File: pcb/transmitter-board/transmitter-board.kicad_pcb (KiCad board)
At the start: 2 copper layers, 0 parts

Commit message: Add transmitter-board schematics
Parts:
- added BT1: Battery, Battery:BatteryHolder_Keystone_1042_1x18650, F.Cu at (60.6, 42.8)
- added C1: 1n, Capacitor_SMD:C_0805_2012Metric_Pad1.18x1.45mm_HandSolder, F.Cu at (45.8, 60.7)
- added C2: 10n, Capacitor_SMD:C_0805_2012Metric_Pad1.18x1.45mm_HandSolder, F.Cu at (45.8, 63.7)
- added C4: 0.1u, Capacitor_SMD:C_0805_2012Metric_Pad1.18x1.45mm_HandSolder, F.Cu at (45.8, 66.7)
- added C6: 0.1u, Capacitor_SMD:C_0805_2012Metric_Pad1.18x1.45mm_HandSolder, F.Cu at (45.8, 69.7)
- added C7: 10u, Capacitor_SMD:C_0805_2012Metric_Pad1.18x1.45mm_HandSolder, F.Cu at (45.8, 72.7)
- added D1: R LED, LED_SMD:LED_0805_2012Metric_Pad1.15x1.40mm_HandSolder, F.Cu at (45.8, 75.8)
- added D2: B LED, LED_SMD:LED_0805_2012Metric_Pad1.15x1.40mm_HandSolder, F.Cu at (45.8, 78.8)
- added D5: IR LED, LED_THT:LED_D1.8mm_W1.8mm_H2.4mm_Horizontal_O3.81mm_Z8.2mm, F.Cu at (25.4, 66.0)
- added J1: USB_C_Receptacle_PowerOnly_6P, Connector_USB:USB_C_Receptacle_GCT_USB4125-xx-x-0190_6P_TopMnt_Horizontal, F.Cu at (54.1, 77.9)
- added Q1: BC817, Package_TO_SOT_SMD:SOT-23, F.Cu at (50.7, 61.6)
- added Q3: AO3400A, Package_TO_SOT_SMD:SOT-23, F.Cu at (50.7, 66.2)
- added Q4: AO3400A, Package_TO_SOT_SMD:SOT-23, F.Cu at (50.7, 70.8)
- added R1: 1k, Resistor_SMD:R_0805_2012Metric_Pad1.20x1.40mm_HandSolder, F.Cu at (36.3, 60.7)
- added R10: 100R, Resistor_SMD:R_0805_2012Metric_Pad1.20x1.40mm_HandSolder, F.Cu at (41.0, 66.6)
- added R11: 18, Resistor_SMD:R_0805_2012Metric_Pad1.20x1.40mm_HandSolder, F.Cu at (41.0, 69.5)
- added R12: 180, Resistor_SMD:R_0805_2012Metric_Pad1.20x1.40mm_HandSolder, F.Cu at (41.0, 72.5)
- added R2: 18.4k, Resistor_SMD:R_0805_2012Metric_Pad1.20x1.40mm_HandSolder, F.Cu at (36.3, 63.6)
- added R3: 5.1k, Resistor_SMD:R_0805_2012Metric_Pad1.20x1.40mm_HandSolder, F.Cu at (36.3, 66.6)
- added R4: 1k, Resistor_SMD:R_0805_2012Metric_Pad1.20x1.40mm_HandSolder, F.Cu at (36.3, 69.5)
- added R5: 1.2k, Resistor_SMD:R_0805_2012Metric_Pad1.20x1.40mm_HandSolder, F.Cu at (36.3, 72.5)
- added R6: 5.1k, Resistor_SMD:R_0805_2012Metric_Pad1.20x1.40mm_HandSolder, F.Cu at (36.3, 75.4)
- added R7: 1k, Resistor_SMD:R_0805_2012Metric_Pad1.20x1.40mm_HandSolder, F.Cu at (41.0, 60.7)
- added R9: 1k, Resistor_SMD:R_0805_2012Metric_Pad1.20x1.40mm_HandSolder, F.Cu at (41.0, 63.6)
- added U1: NE555D, Package_SO:SOIC-8_3.9x4.9mm_P1.27mm, F.Cu at (57.3, 62.5)
- added U3: TP4056-42-ESOP8, Package_SO:SOIC-8-1EP_3.9x4.9mm_P1.27mm_EP2.41x3.3mm_ThermalVias, F.Cu at (57.3, 69.1)
- added U4: DW01A, Package_TO_SOT_SMD:SOT-23-6, F.Cu at (36.5, 79.3)

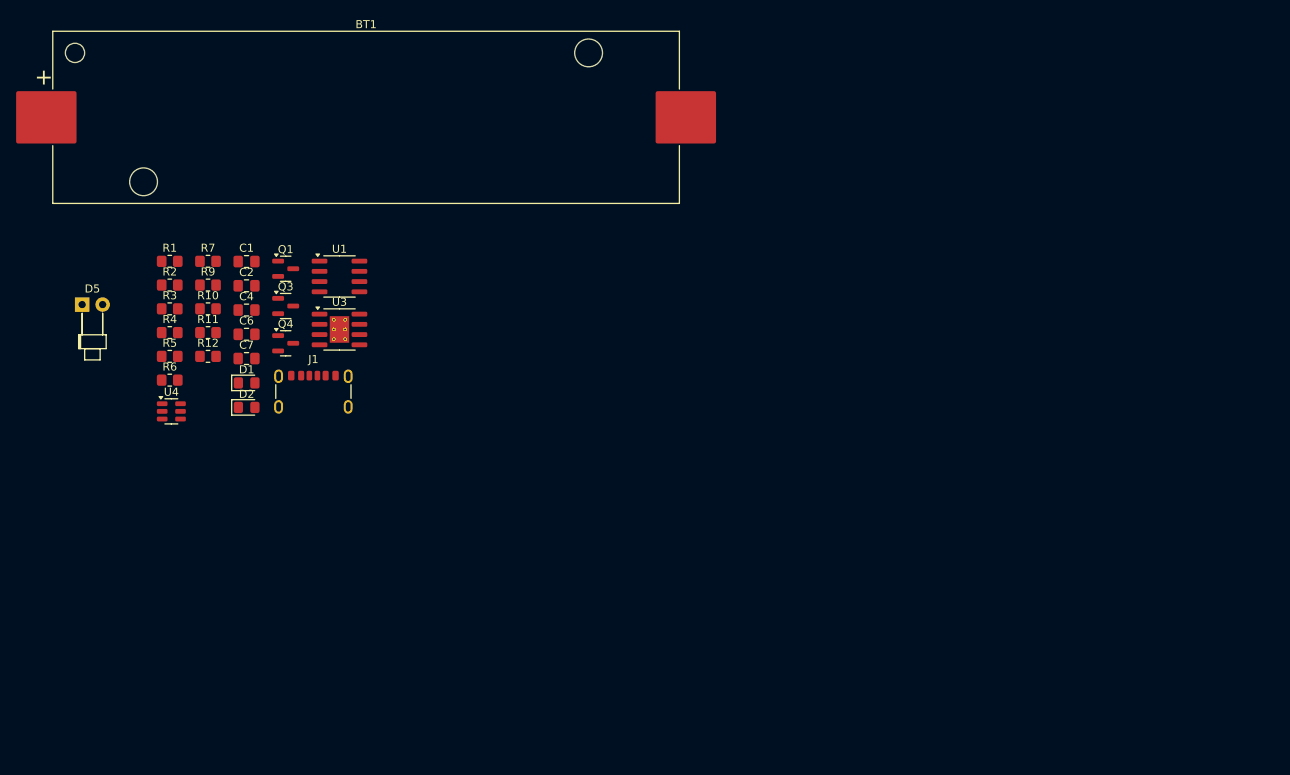
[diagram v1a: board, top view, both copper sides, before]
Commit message: Add transmitter-board pcb
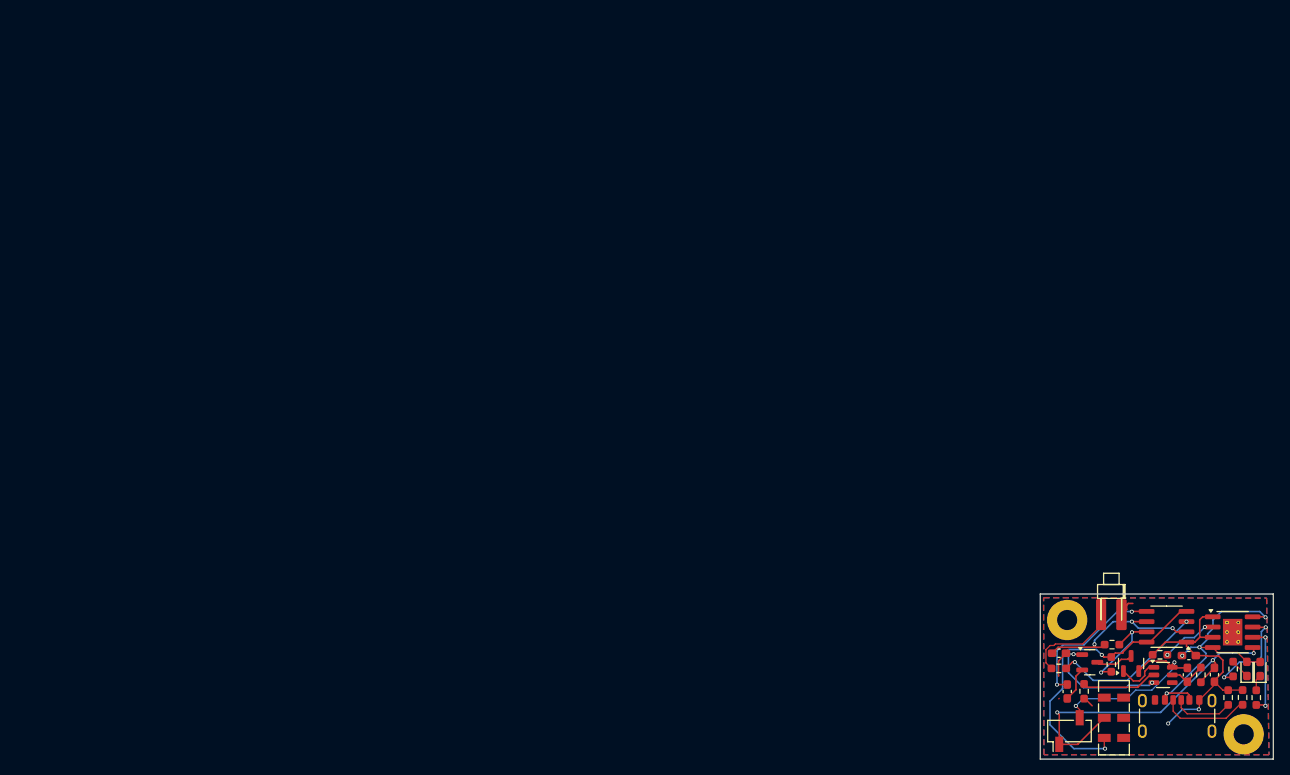
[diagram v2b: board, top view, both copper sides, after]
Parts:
- removed D5: IR LED, LED_THT:LED_D1.8mm_W1.8mm_H2.4mm_Horizontal_O3.81mm_Z8.2mm
- removed Q1: BC817, Package_TO_SOT_SMD:SOT-23
- removed R11: 18, Resistor_SMD:R_0805_2012Metric_Pad1.20x1.40mm_HandSolder
- removed R12: 180, Resistor_SMD:R_0805_2012Metric_Pad1.20x1.40mm_HandSolder
- added D3: IR LED, LED_THT:LED_THT_Horizontal_SMD_mounted, F.Cu at (154.4, 106.3)
- added R8: 150, Resistor_SMD:R_0603_1608Metric_Pad0.98x0.95mm_HandSolder, F.Cu at (146.6, 111.2)
- added REF**: MountingHole_2.5mm_Pad, MountingHole:MountingHole_2.5mm_Pad, F.Cu at (147.7, 105.2)
- added REF**: MountingHole_2.5mm_Pad, MountingHole:MountingHole_2.5mm_Pad, F.Cu at (169.6, 119.4)
- added SW1: SW_DPDT_x2, Button_Switch_SMD:SW_DPDT_CK_JS202011JCQN, F.Cu at (153.5, 117.3)
- BT1: footprint Battery:BatteryHolder_Keystone_1042_1x18650 -> Connector_PinSocket_2.54mm:PinSocket_1x02_P2.54mm_Vertical_SMD_Pin1Left
- C1, C2, C4, C6, C7: footprint Capacitor_SMD:C_0805_2012Metric_Pad1.18x1.45mm_HandSolder -> Capacitor_SMD:C_0603_1608Metric_Pad1.08x0.95mm_HandSolder
- D1, D2: footprint LED_SMD:LED_0805_2012Metric_Pad1.15x1.40mm_HandSolder -> LED_SMD:LED_0603_1608Metric_Pad1.05x0.95mm_HandSolder
- R1, R10, R2, R3, R4, R5, R6, R7, R9: footprint Resistor_SMD:R_0805_2012Metric_Pad1.20x1.40mm_HandSolder -> Resistor_SMD:R_0603_1608Metric_Pad0.98x0.95mm_HandSolder
- moved R4 142.3 mm to (171.1, 114.8), turned to 90 degrees
- moved R3 140.0 mm to (167.6, 114.8), turned to 90 degrees
- moved R6 138.9 mm to (169.4, 114.8), turned to 90 degrees
- moved R7 136.9 mm to (168.3, 111.3), turned to 90 degrees
- moved R10 131.3 mm to (164.3, 112.0), turned to 90 degrees
- moved D2 129.9 mm to (171.6, 111.3), turned to 90 degrees
- moved D1 129.1 mm to (170.0, 111.3), turned to 90 degrees
- moved R5 128.4 mm to (159.2, 109.5), turned to 180 degrees
- moved U4 127.4 mm to (159.6, 112.0)
- moved R1 127.1 mm to (153.1, 110.7), turned to -90 degrees
- moved C7 126.4 mm to (165.9, 112.0), turned to -90 degrees
- moved R2 125.2 mm to (153.2, 108.3), turned to 180 degrees
- moved C4 124.6 mm to (162.8, 109.6)
- moved C6 124.2 mm to (162.6, 112.0), turned to 90 degrees
- moved R9 119.9 mm to (149.8, 114.0), turned to -90 degrees
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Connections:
- BT1 pad 2: GND -> /B-
- C6 pad 2: GND -> /B-
- J1 pad S1: unconnected-(J1-SHIELD-PadS1) -> GND
- Q4 pad 2: GND -> /B-
- R1 pad 1: +3V8 -> Net-(SW1A-A)
- U1 pad 4: +3V8 -> Net-(SW1A-A)
- U1 pad 8: +3V8 -> Net-(SW1A-A)
- U4 pad 6: GND -> /B-
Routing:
- net GND: track 0.00 -> 45.2 mm, vias 0 -> 2
- net +3V8: track 0.00 -> 42.8 mm, vias 0 -> 3
- net Net-(SW1A-A): track 0.00 -> 37.2 mm, vias 0 -> 2
- net /IN+: track 0.00 -> 36.6 mm, vias 0 -> 4
- net /B-: track 0.00 -> 24.2 mm, vias 0 -> 2
- net Net-(U1-THR): track 0.00 -> 23.0 mm, vias 0 -> 3
- net /555OUT: track 0.00 -> 19.2 mm, vias 0 -> 2
- net Net-(U1-CV): track 0.00 -> 18.7 mm, vias 0 -> 2
- net Net-(Q3-G): track 0.00 -> 15.5 mm, vias 0 -> 2
- net Net-(U3-~{CHRG}): track 0.00 -> 12.4 mm, vias 0 -> 2
- net Net-(D3-A): track 0.00 -> 12.1 mm
- net Net-(U1-DIS): track 0.00 -> 11.9 mm, vias 0 -> 2
- net Net-(U3-~{STDBY}): track 0.00 -> 11.3 mm, vias 0 -> 2
- net Net-(J1-CC1): track 0.00 -> 11.1 mm
- net Net-(U4-CS): track 0.00 -> 9.47 mm
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- added copper zone on B.Cu, net GND
- added copper zone on F.Cu, net GND
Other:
- board outline added: 28.9 x 20.5 mm

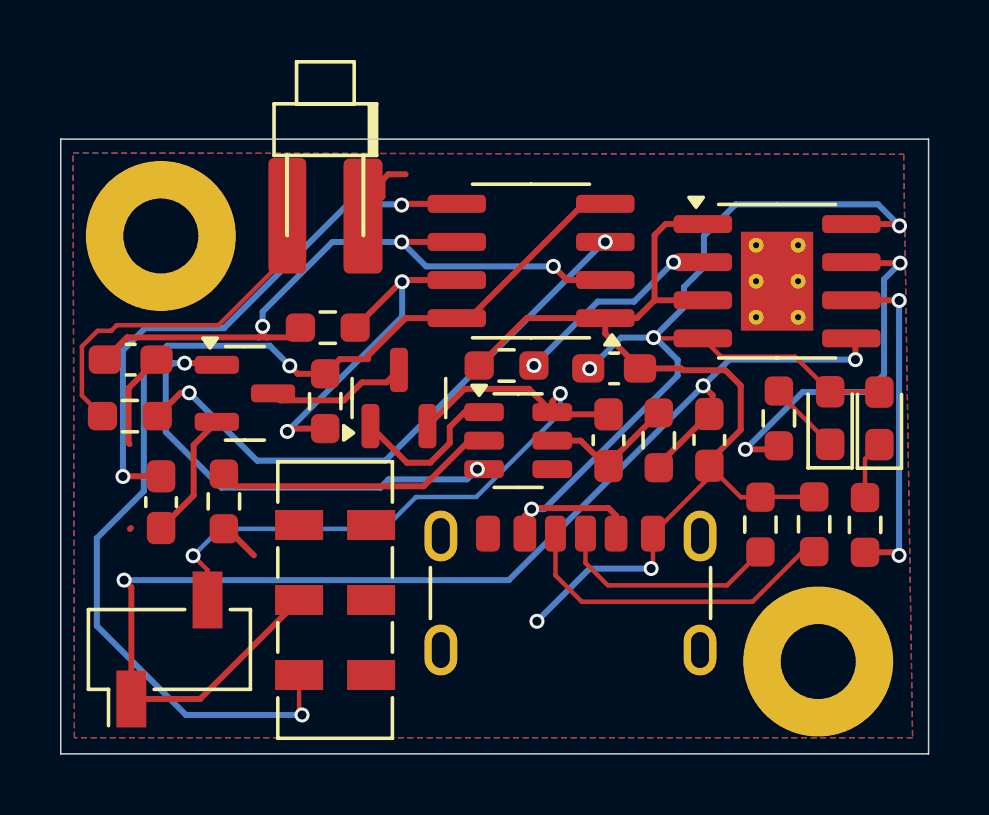
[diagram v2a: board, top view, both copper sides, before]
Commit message: Change hole size under TP4056 and change battery connector to THT.
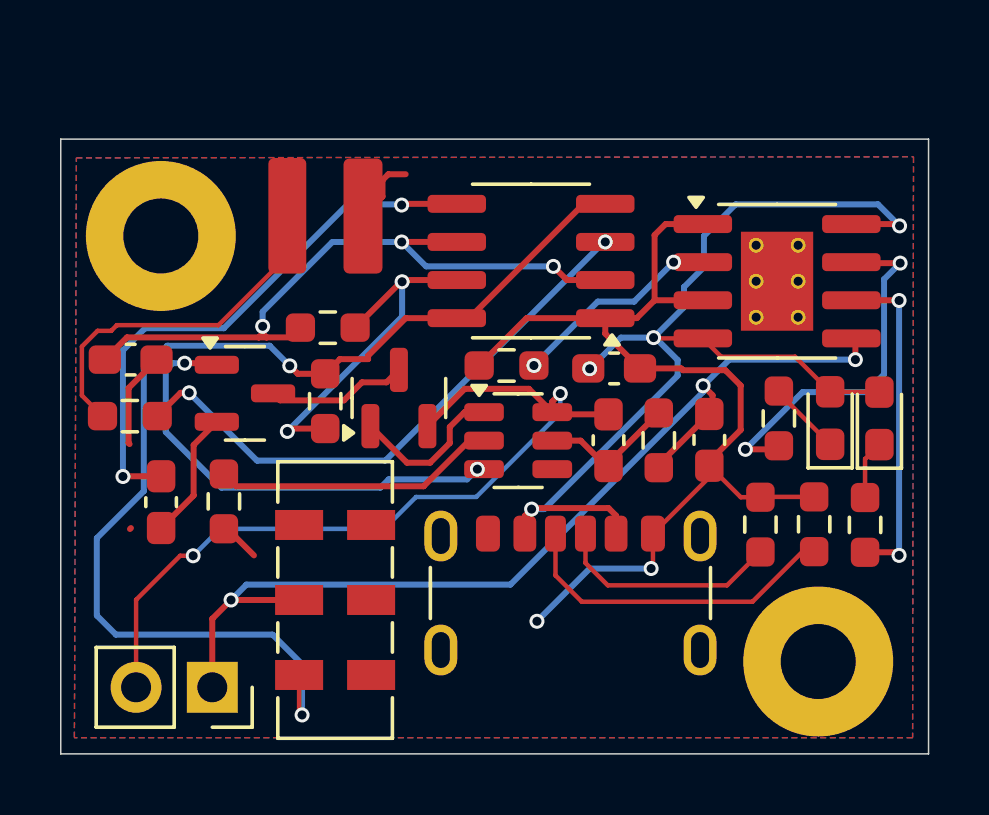
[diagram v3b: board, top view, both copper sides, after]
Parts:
- BT1: footprint Connector_PinSocket_2.54mm:PinSocket_1x02_P2.54mm_Vertical_SMD_Pin1Left -> Connector_PinSocket_2.54mm:PinSocket_1x02_P2.54mm_Vertical
- moved BT1 1.91 mm to (149.4, 120.2), turned to -90 degrees
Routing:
- net +3V8: track 42.8 -> 34.1 mm
- net /B-: track 24.2 -> 27.9 mm
- net Net-(SW1A-A): track 37.2 -> 38.0 mm

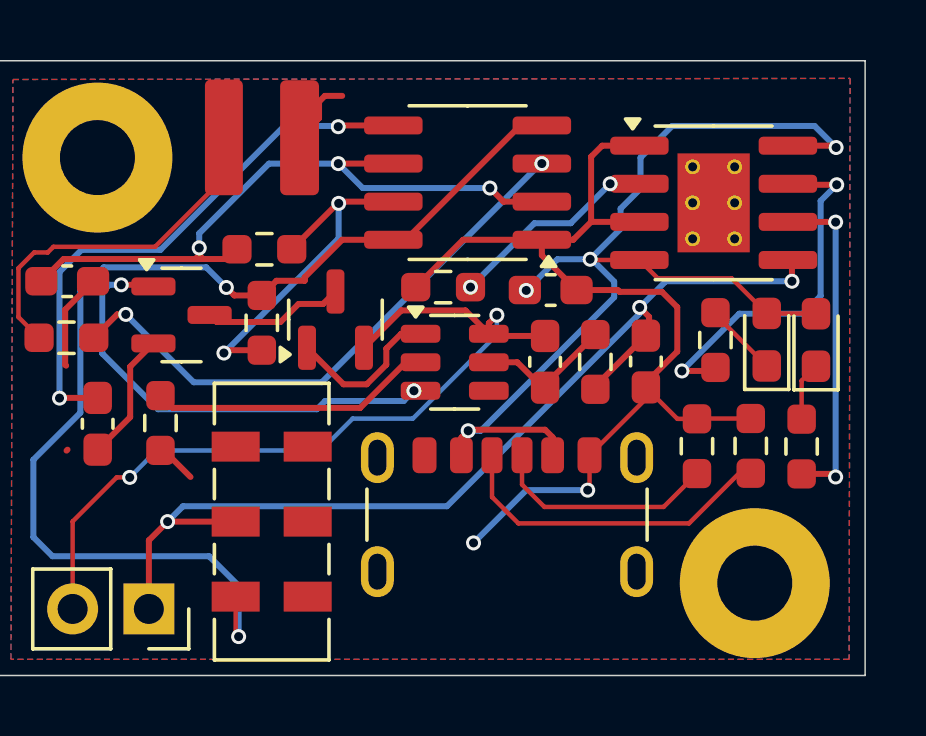
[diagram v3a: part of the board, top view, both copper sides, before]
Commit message: Change USB and battery connector
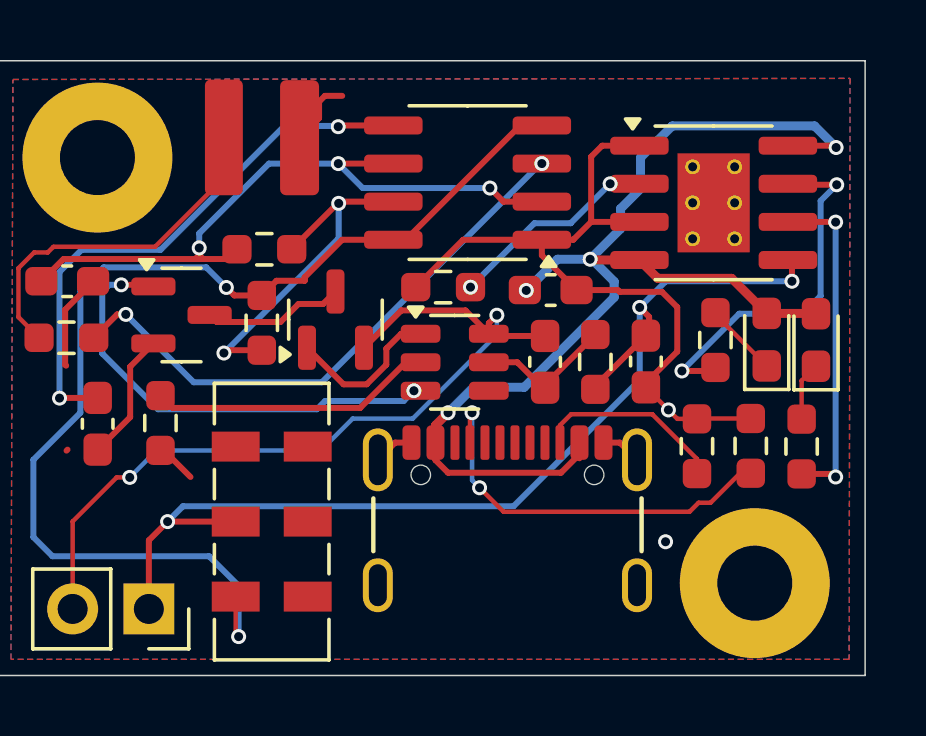
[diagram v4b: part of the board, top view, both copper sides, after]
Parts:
- J1: value USB_C_Receptacle_PowerOnly_6P -> USB-C_USB-310F-B-SU; footprint Connector_USB:USB_C_Receptacle_GCT_USB4125-xx-x-0190_6P_TopMnt_Horizontal -> DW-footprints:USB-C-Receptacle_USB-310-B-SU
- moved J1 0.18 mm to (161.3, 118.4)
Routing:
- net GND: track 45.2 -> 39.5 mm
- net /IN+: track 36.6 -> 41.0 mm
- net Net-(J1-CC1): track 11.1 -> 13.9 mm, vias 0 -> 2
- net +3V8: track 34.1 -> 35.4 mm
- net Net-(J1-CC2): track 7.58 -> 6.40 mm
